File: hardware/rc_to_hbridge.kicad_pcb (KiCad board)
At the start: 2 copper layers, 40 x 32 mm, 17 parts, among them CON1 AVR-ISP-6, IC1 ATMEGA328-A, P1 CONN_01X03, P2 CONN_01X03, P3 CONN_01X06, Y1 16Mhz

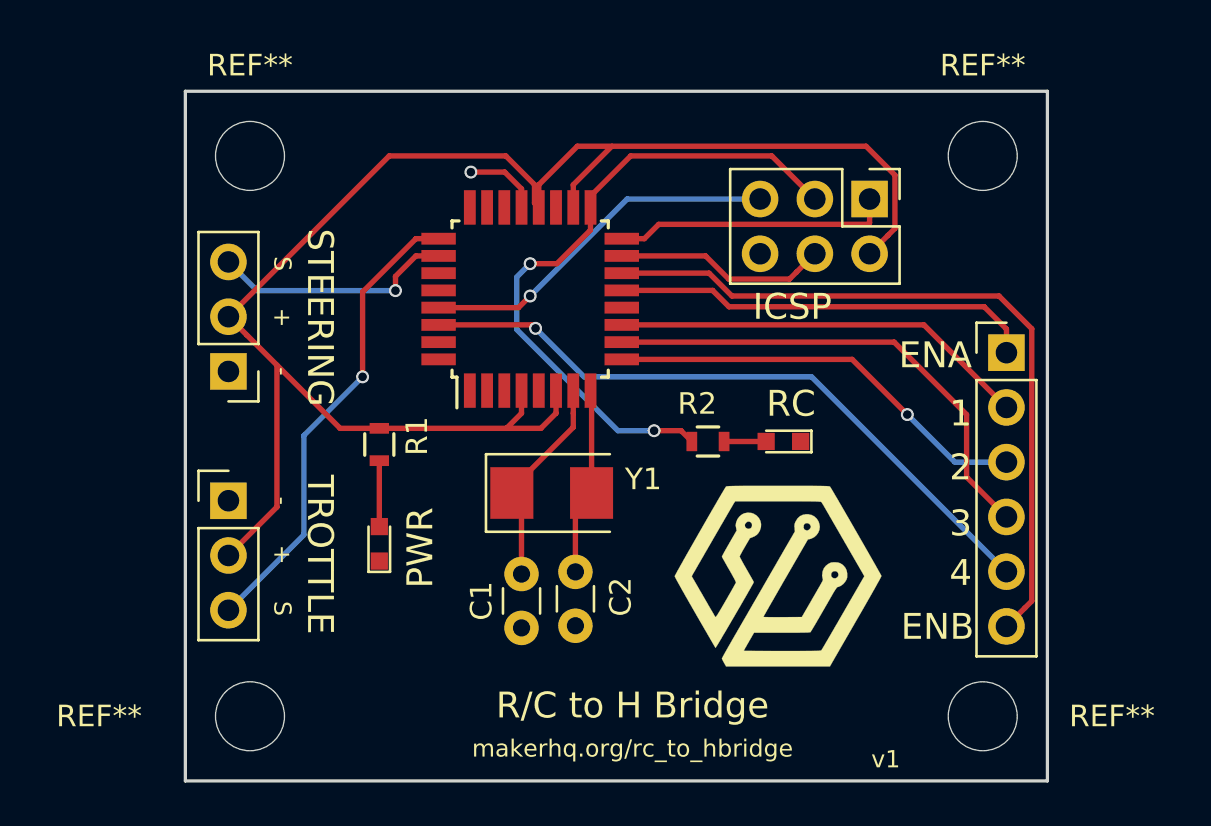
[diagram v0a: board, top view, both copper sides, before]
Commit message: New PCB with aux out and serial. Updated firmware to match.
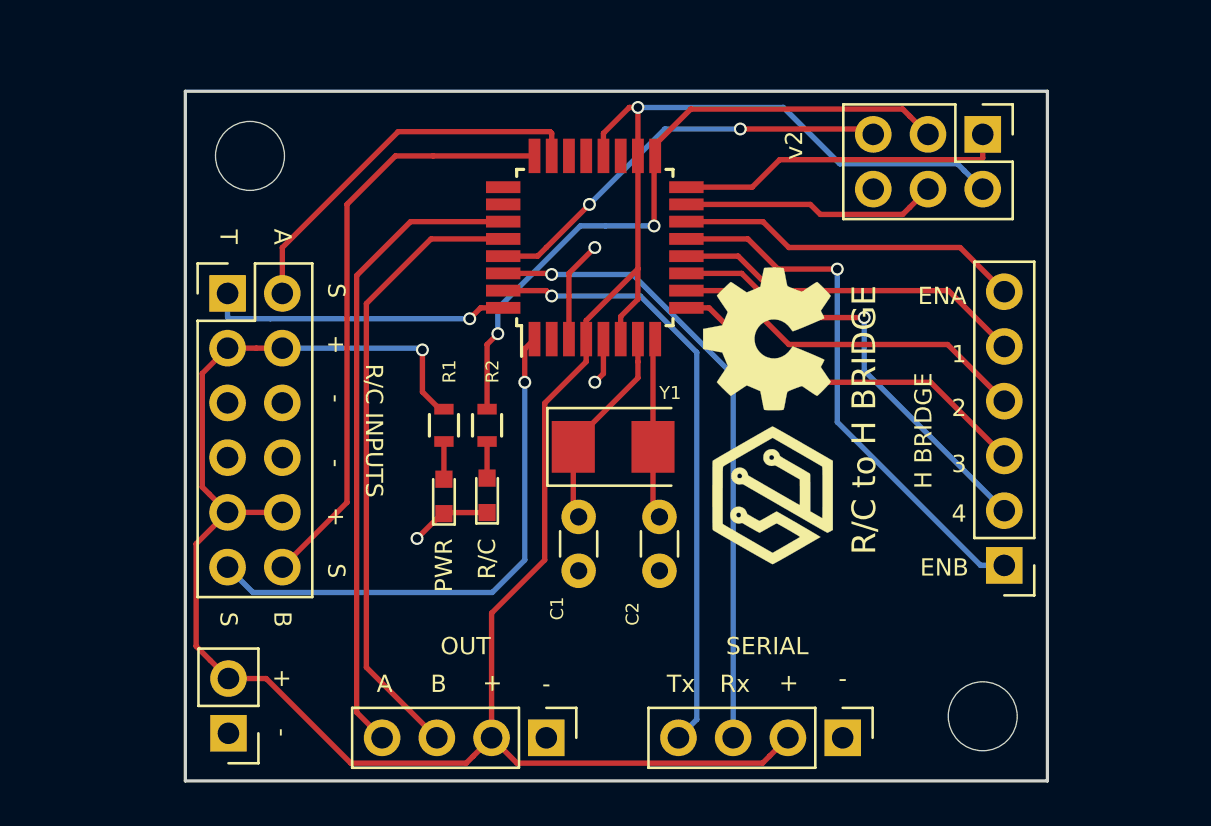
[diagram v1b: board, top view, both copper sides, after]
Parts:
- removed the G*** at (149.5, 105.5)
- removed the REF** at (125.0, 112.0)
- removed the REF** at (159.0, 86.0)
- added G***: LOGO, machadolab:mhq_logo_small, F.Cu at (149.2, 101.8)
- added P4: CONN_01X06, Pin_Headers:Pin_Header_Straight_1x06_Pitch2.54mm, F.Cu at (160.0, 105.0)
- added P5: CONN_01X04, Pin_Headers:Pin_Header_Straight_1x04_Pitch2.54mm, F.Cu at (138.8, 113.0)
- added REF***: OSHW-Symbol_6.7x6mm_SilkScreen, Symbols:OSHW-Symbol_6.7x6mm_SilkScreen, F.Cu at (149.0, 94.5)
- P1: value CONN_01X03 -> CONN_01X04; footprint Pin_Headers:Pin_Header_Straight_1x03_Pitch2.54mm -> Pin_Headers:Pin_Header_Straight_1x04_Pitch2.54mm
- P2: value CONN_01X03 -> CONN_01X02; footprint Pin_Headers:Pin_Header_Straight_1x03_Pitch2.54mm -> Pin_Headers:Pin_Header_Straight_1x02_Pitch2.54mm
- P3: value CONN_01X06 -> CONN_02X06; footprint Pin_Headers:Pin_Header_Straight_1x06_Pitch2.54mm -> Pin_Headers:Pin_Header_Straight_2x06_Pitch2.54mm
- moved P3 36.2 mm to (124.0, 92.4)
- moved P1 30.5 mm to (152.5, 113.0), turned to 270 degrees
- moved P2 16.8 mm to (124.0, 112.8)
- moved D2 14.0 mm to (136.0, 101.8), turned to 90 degrees
- moved R2 10.3 mm to (136.0, 98.5), turned to 90 degrees
- moved CON1 6.05 mm to (159.0, 85.0)
- moved C2 4.66 mm to (144.0, 105.2)
- moved IC1 3.84 mm to (141.0, 90.2)
- moved C1 3.75 mm to (140.2, 105.2)
- moved D1 3.72 mm to (134.0, 101.8)
- moved Y1 3.56 mm to (141.8, 99.5)
- moved R1 3.13 mm to (134.0, 98.5)
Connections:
- IC1 pad 1: (no net) -> /RC_S
- IC1 pad 12: (no net) -> /L_FWD
- IC1 pad 23: (no net) -> /RC_A
- IC1 pad 24: (no net) -> /RC_B
- IC1 pad 25: /RC_T -> (no net)
- IC1 pad 26: /RC_S -> (no net)
- IC1 pad 27: (no net) -> /OUT_A
- IC1 pad 28: (no net) -> /OUT_B
- IC1 pad 30: /L_FWD -> /RX
- IC1 pad 31: (no net) -> /TX
- IC1 pad 32: (no net) -> /RC_T
- P1 pad 3: /RC_T -> /RX
- P3 pad 1: /R_EN -> /RC_T
- P3 pad 2: /R_FWD -> /RC_A
- P3 pad 3: /R_REV -> VCC
- P3 pad 4: /L_REV -> VCC
- P3 pad 5: /L_FWD -> GND
- P3 pad 6: /L_EN -> GND
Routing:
- net VCC: track 76.0 -> 117.8 mm, vias 0 -> 2
- net /OUT_A: track 0.00 -> 29.8 mm
- net /RX: track 0.00 -> 29.5 mm, vias 0 -> 1
- net /OUT_B: track 0.00 -> 28.5 mm
- net /TX: track 0.00 -> 28.4 mm, vias 0 -> 1
- net /RC_B: track 0.00 -> 27.7 mm
- net /L_EN: track 34.4 -> 16.1 mm
- net /RC_A: track 0.00 -> 17.9 mm
- net /L_FWD: track 31.1 -> 16.5 mm, vias 1 -> 0
- net /RC_S: track 11.4 -> 25.3 mm
- net /RC_T: track 21.9 -> 14.1 mm
- net GND: track 3.53 -> 10.7 mm, vias 1 -> 3
- net /L_REV: track 22.9 -> 16.9 mm
- net /R_EN: track 19.7 -> 25.2 mm, vias 0 -> 1
- net /RST: track 17.0 -> 19.7 mm, vias 1 -> 2
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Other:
- board text added: "A"
- board text added: "B"
- board text added: "H BRIDGE"
- board text added: "OUT"
- board text added: "R/C"
- board text added: "R/C INPUTS"
- board text added: "R/C to H BRIDGE"
- board text added: "Rx"
- board text added: "SERIAL"
- board text added: "T"
- board text added: "Tx"
- board text added: "v2"
- board text removed: "ICSP"
- board text removed: "R/C to H Bridge"
- board text removed: "RC"
- board text removed: "STEERING"
- board text removed: "TROTTLE"
- board text removed: "makerhq.org/rc_to_hbridge"
- board text removed: "v1"

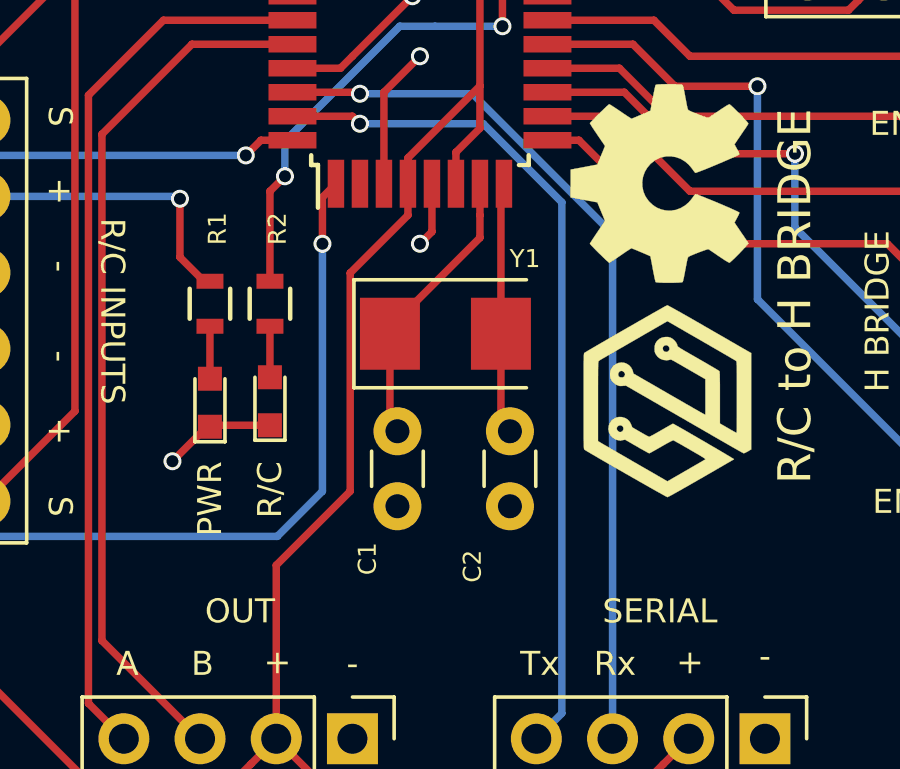
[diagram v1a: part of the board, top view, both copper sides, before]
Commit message: fix footprints and better handle no rc
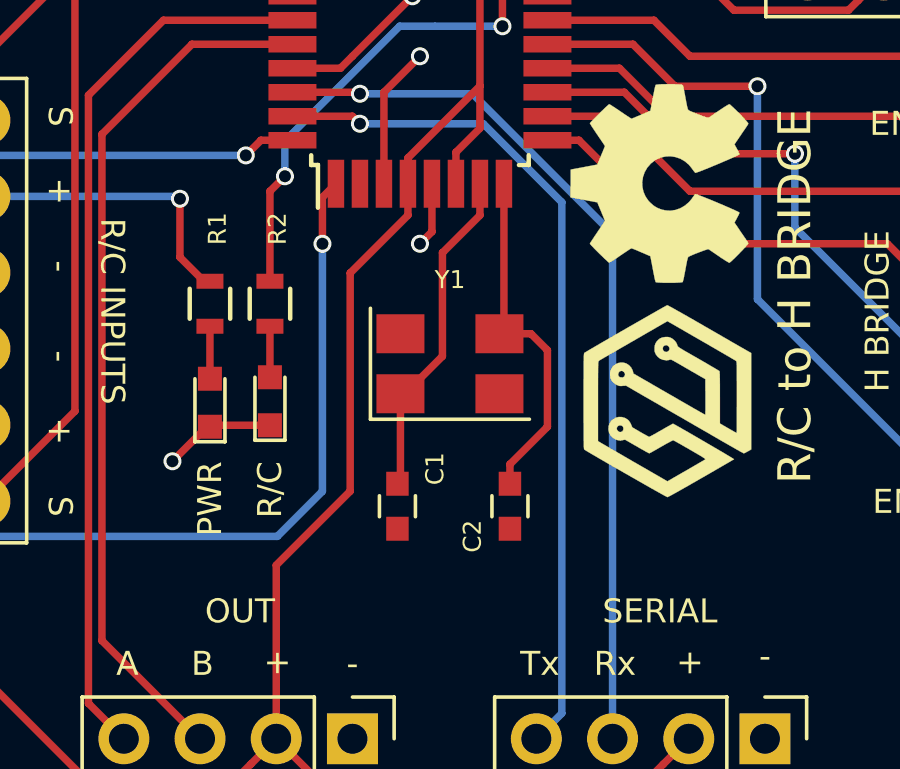
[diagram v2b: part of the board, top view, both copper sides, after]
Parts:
- C1, C2: footprint Capacitors_THT:C_Disc_D3.0mm_W1.6mm_P2.50mm -> Capacitors_SMD:C_0603
- Y1: value 16Mhz -> Crystal_GND24; footprint Crystals:Crystal_SMD_5032-2pin_5.0x3.2mm -> Crystals:Crystal_SMD_5032-4pin_5.0x3.2mm
- moved Y1 1.01 mm to (142.0, 100.5)
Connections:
- Y1 pad 2: Net-(C2-Pad2) -> GND
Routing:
- net Net-(C2-Pad2): track 8.42 -> 12.0 mm
- net Net-(C1-Pad2): track 9.60 -> 11.2 mm

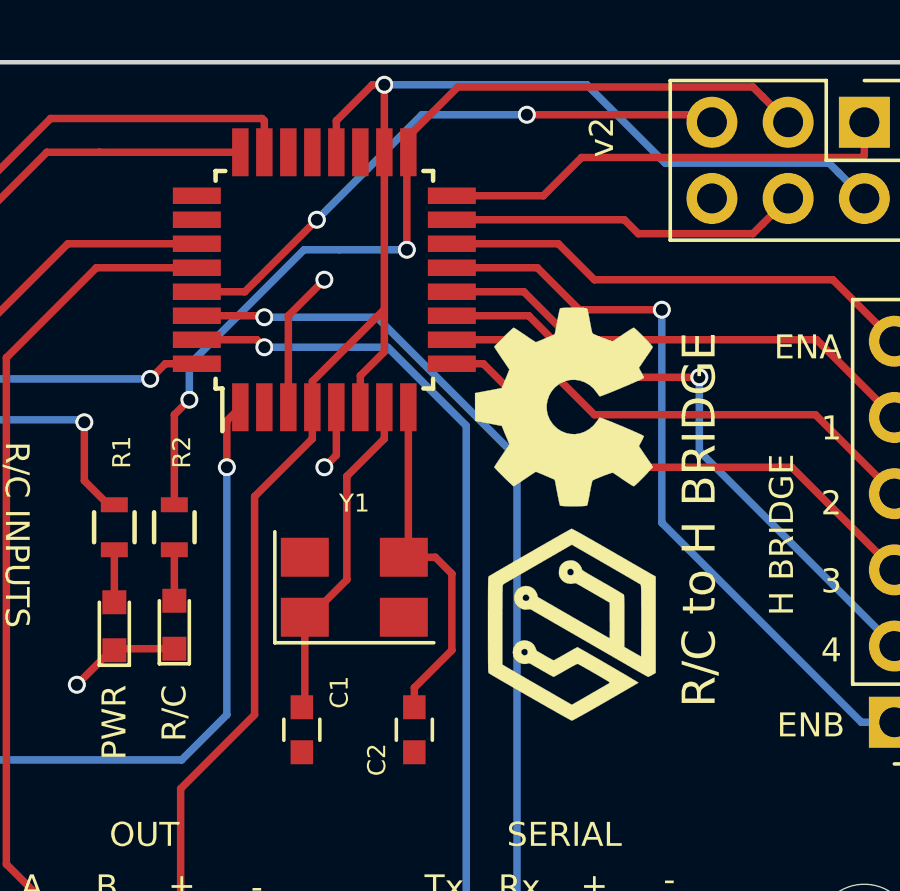
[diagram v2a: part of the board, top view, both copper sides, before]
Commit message: update hardware design for manufacturing - convert to kicad
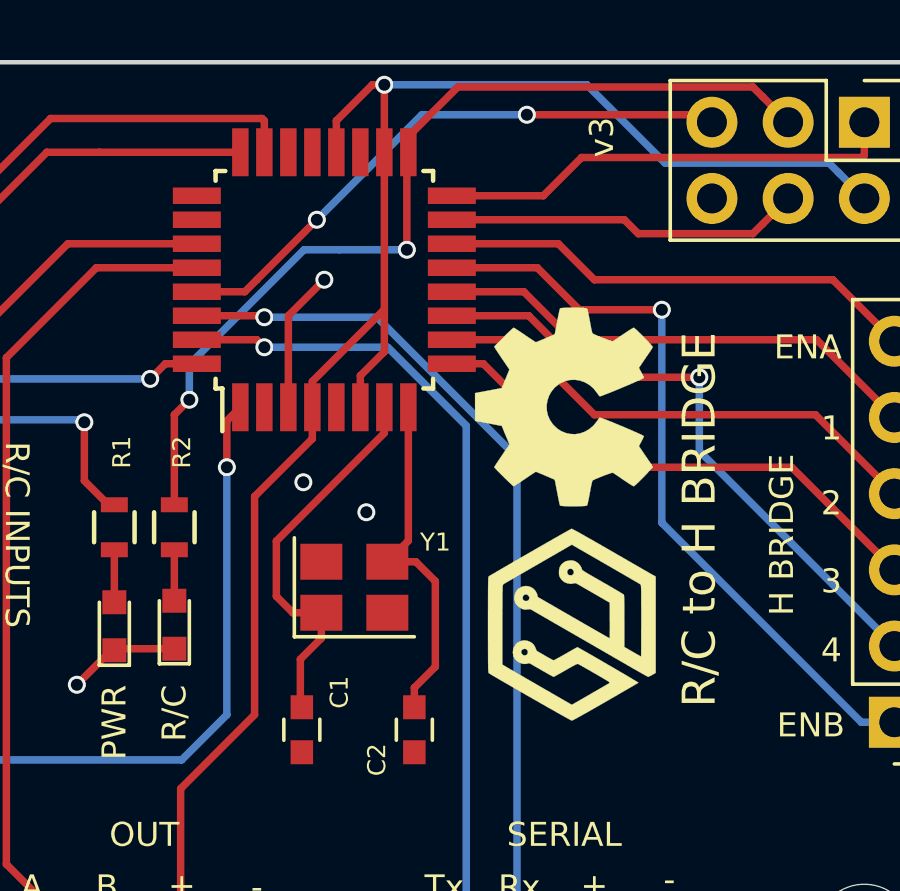
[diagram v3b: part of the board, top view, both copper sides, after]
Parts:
- Y1: footprint Crystals:Crystal_SMD_5032-4pin_5.0x3.2mm -> Crystal:Crystal_SMD_3225-4Pin_3.2x2.5mm
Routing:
- net GND: track 10.7 -> 8.49 mm, vias 3 -> 4
- net Net-(C1-Pad2): track 11.2 -> 13.0 mm
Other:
- board text added: "v3"
- board text removed: "v2"
